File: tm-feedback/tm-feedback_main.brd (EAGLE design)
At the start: 60.1 x 40.3 mm, 45 parts

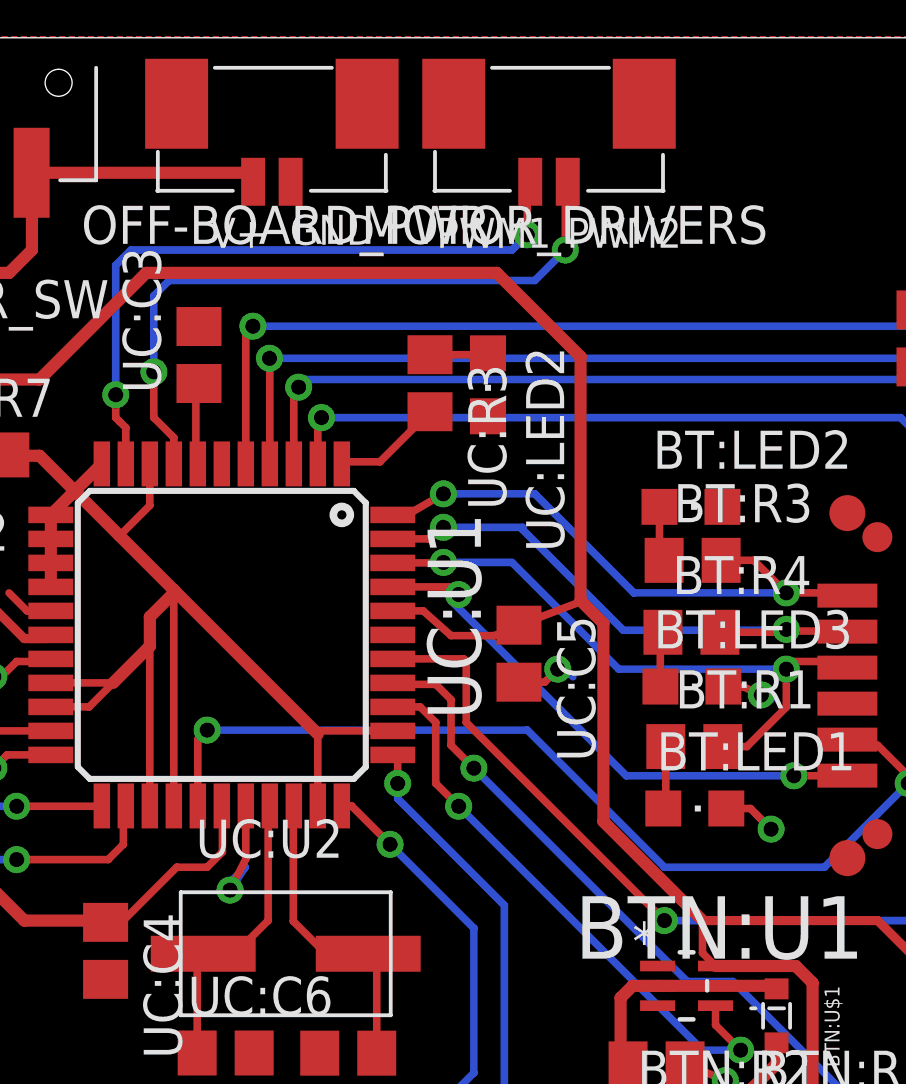
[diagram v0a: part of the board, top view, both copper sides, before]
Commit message: Fix ground vias
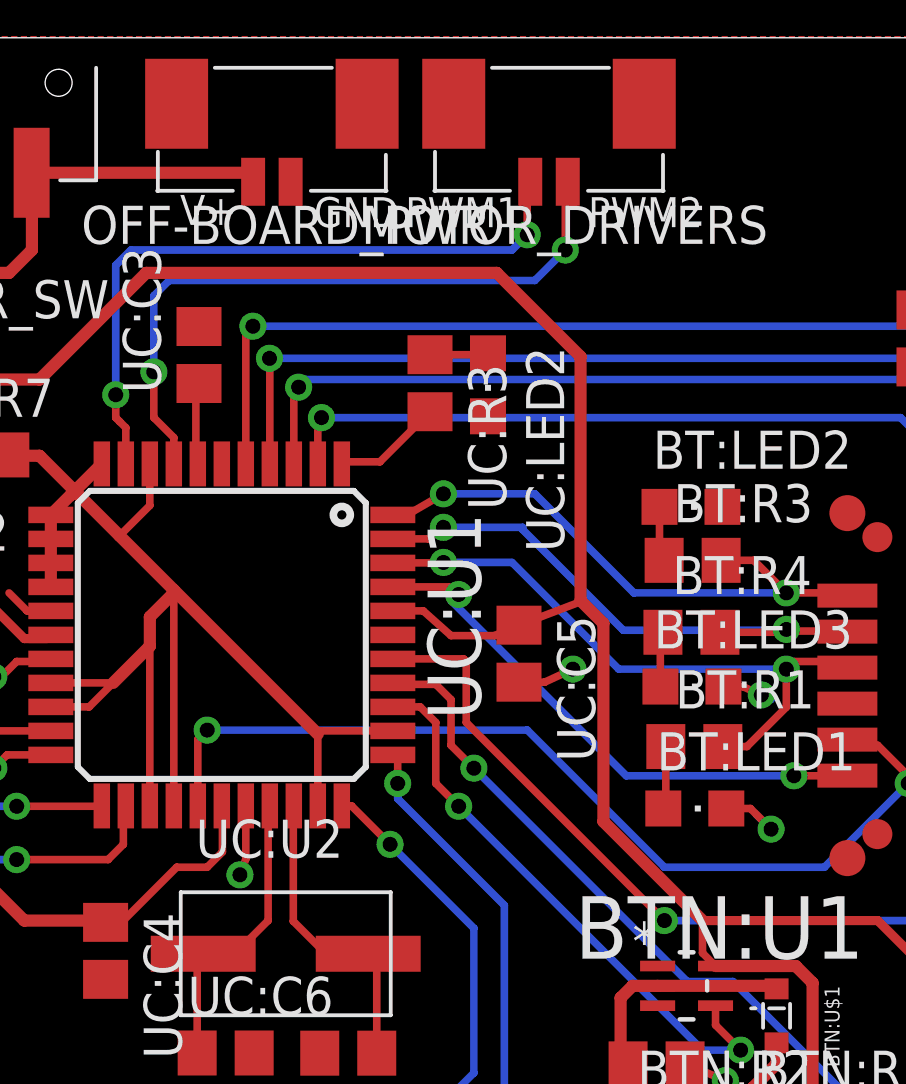
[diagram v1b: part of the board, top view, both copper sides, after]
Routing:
- net GND: track 21.6 -> 19.2 mm
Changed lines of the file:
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@@
 <setting verticaltext="up"/>
 </settings>
-<grid distance="10" unitdist="mil" unit="mil" style="lines" multiple="10" display="yes" altdistance="0.01" altunitdist="mm" altunit="mm"/>
+<grid distance="1" unitdist="mil" unit="mil" style="lines" multiple="10" display="yes" altdistance="0.01" altunitdist="mm" altunit="mm"/>
 <layers>
 <layer number="1" name="Top" color="4" fill="1" visible="yes" active="yes"/>
@@
 <wire x1="60.122" y1="40.348" x2="0" y2="40.348" width="0" layer="20"/>
 <wire x1="0" y1="40.348" x2="0" y2="0" width="0" layer="20"/>
-<text x="24.24" y="33.348" size="1" layer="21" font="vector" ratio="20">V+</text>
-<text x="26.886" y="33.448" size="1" layer="21" font="vector" ratio="20">GND</text>
-<text x="31.778" y="33.348" size="1" layer="21" font="vector" ratio="20">PWM1</text>
-<text x="36.124" y="33.348" size="1" layer="21" font="vector" ratio="20">PWM2</text>
+<text x="23.224" y="34.11" size="1" layer="21" font="vector" ratio="20">V+</text>
+<text x="27.686" y="34.036" size="1" layer="21" font="vector" ratio="20">GND</text>
+<text x="30.734" y="34.036" size="1" layer="21" font="vector" ratio="20">PWM1</text>
+<text x="36.83" y="34.036" size="1" layer="21" font="vector" ratio="20">PWM2</text>
 <text x="5.554" y="34.65" size="1" layer="21" font="vector" ratio="20">+</text>
 <text x="5.5" y="31.192" size="1" layer="21" font="vector" ratio="20">-</text>
@@
 </polygon>
 <wire x1="25.418" y1="14.744" x2="25.418" y2="12.972" width="0.254" layer="1"/>
-<wire x1="25.418" y1="12.972" x2="24.892" y2="11.938" width="0.254" layer="1"/>
-<via x="24.892" y="11.938" extent="1-16" drill="0.5"/>
-<wire x1="24.892" y1="11.938" x2="25.4" y2="12.7" width="0.254" layer="16"/>
-<wire x1="25.4" y1="12.7" x2="24.892" y2="12.192" width="0.254" layer="16"/>
+<wire x1="25.418" y1="12.972" x2="25.2222" y2="12.446" width="0.254" layer="1"/>
+<via x="25.2222" y="12.446" extent="1-16" drill="0.5"/>
 <wire x1="15.652" y1="26.444" x2="15.652" y2="26.32" width="0.254" layer="1"/>
 <wire x1="15.652" y1="26.32" x2="14.478" y2="25.146" width="0.254" layer="1"/>
@@
 <wire x1="41.402" y1="5.588" x2="41.656" y2="5.334" width="0.254" layer="16"/>
 <wire x1="34.524" y1="18.868" x2="35.378" y2="18.868" width="0.254" layer="1"/>
-<wire x1="35.378" y1="18.868" x2="35.814" y2="19.304" width="0.254" layer="1"/>
-<via x="35.814" y="19.304" extent="1-16" drill="0.5"/>
-<wire x1="35.814" y1="19.304" x2="36.068" y2="19.304" width="0.254" layer="16"/>
-<wire x1="36.068" y1="19.304" x2="36.322" y2="19.05" width="0.254" layer="16"/>
+<wire x1="35.378" y1="18.868" x2="36.322" y2="19.304" width="0.254" layer="1"/>
+<via x="36.322" y="19.304" extent="1-16" drill="0.5"/>
 <wire x1="41.434" y1="14.658" x2="42.238" y2="14.658" width="0.254" layer="1"/>
 <wire x1="42.238" y1="14.658" x2="42.926" y2="13.97" width="0.254" layer="1"/>

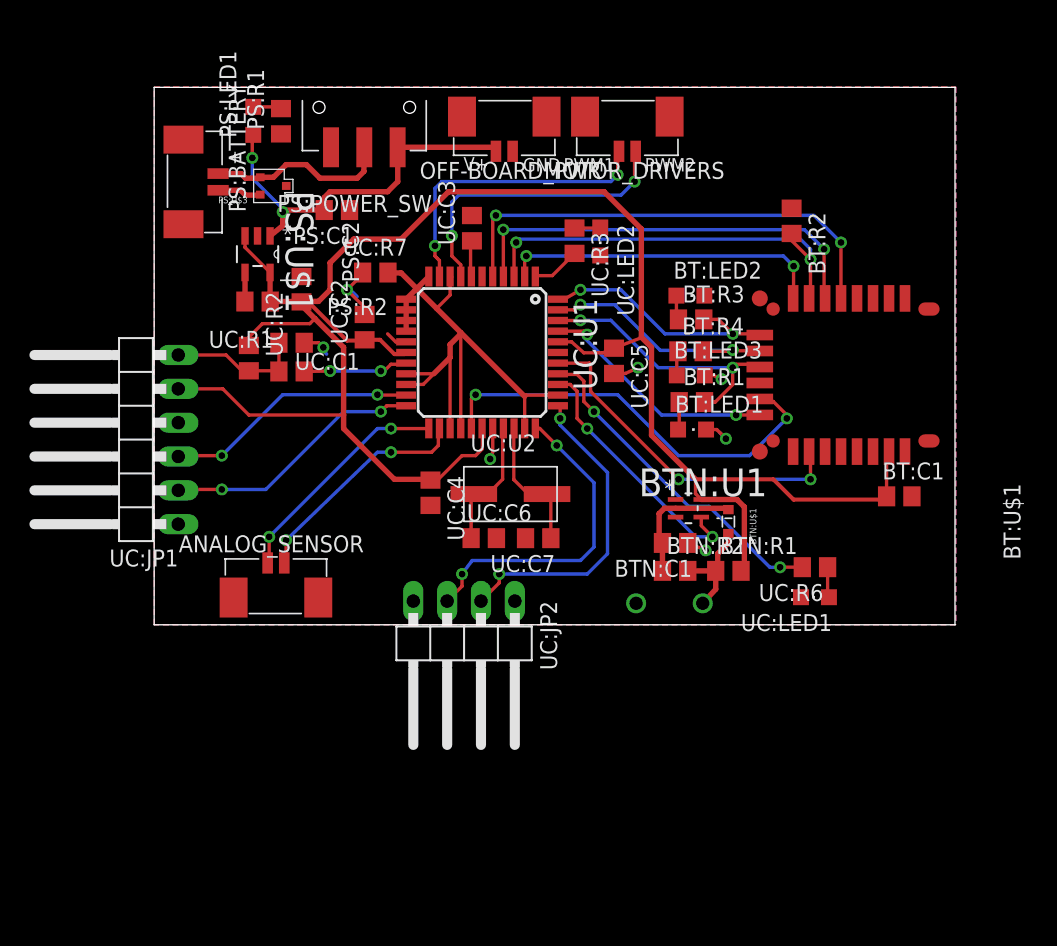
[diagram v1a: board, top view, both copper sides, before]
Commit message: Fix more ground vias
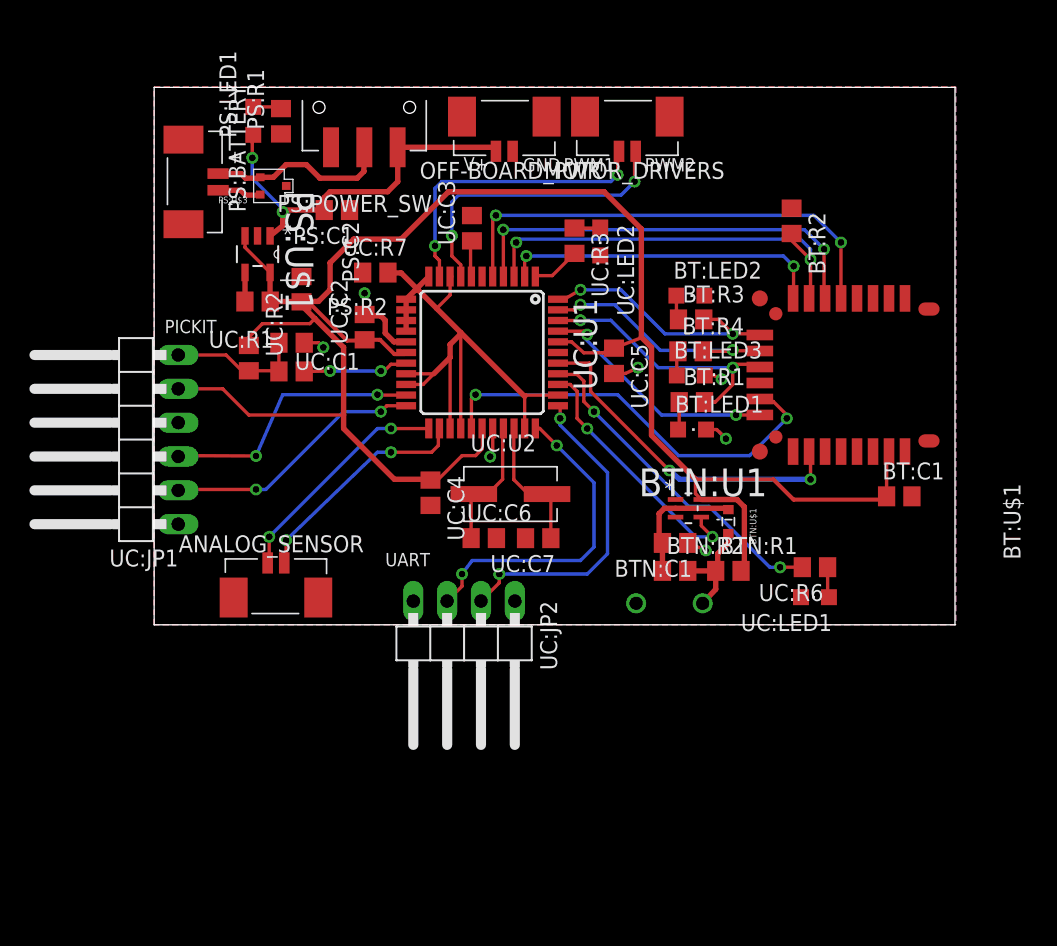
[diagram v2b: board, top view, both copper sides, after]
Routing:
- net GND: track 19.2 -> 16.8 mm
- net UC:PGD: track 19.0 -> 20.2 mm
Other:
- board text added: "PICKIT"
- board text added: "UART"
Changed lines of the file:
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@@
 <layer number="20" name="Dimension" color="15" fill="1" visible="yes" active="yes"/>
 <layer number="21" name="tPlace" color="7" fill="1" visible="yes" active="yes"/>
-<layer number="22" name="bPlace" color="7" fill="1" visible="yes" active="yes"/>
+<layer number="22" name="bPlace" color="7" fill="1" visible="no" active="yes"/>
 <layer number="23" name="tOrigins" color="15" fill="1" visible="no" active="yes"/>
 <layer number="24" name="bOrigins" color="15" fill="1" visible="no" active="yes"/>
@@
 <layer number="27" name="tValues" color="7" fill="1" visible="no" active="yes"/>
 <layer number="28" name="bValues" color="7" fill="1" visible="no" active="yes"/>
-<layer number="29" name="tStop" color="7" fill="3" visible="no" active="yes"/>
+<layer number="29" name="tStop" color="7" fill="3" visible="yes" active="yes"/>
 <layer number="30" name="bStop" color="7" fill="6" visible="no" active="yes"/>
 <layer number="31" name="tCream" color="7" fill="4" visible="no" active="yes"/>
@@
 <layer number="38" name="bTest" color="7" fill="1" visible="no" active="yes"/>
 <layer number="39" name="tKeepout" color="4" fill="11" visible="yes" active="yes"/>
-<layer number="40" name="bKeepout" color="1" fill="11" visible="yes" active="yes"/>
+<layer number="40" name="bKeepout" color="1" fill="11" visible="no" active="yes"/>
 <layer number="41" name="tRestrict" color="4" fill="10" visible="yes" active="yes"/>
-<layer number="42" name="bRestrict" color="1" fill="10" visible="yes" active="yes"/>
-<layer number="43" name="vRestrict" color="2" fill="10" visible="yes" active="yes"/>
-<layer number="44" name="Drills" color="7" fill="1" visible="yes" active="yes"/>
-<layer number="45" name="Holes" color="7" fill="1" visible="yes" active="yes"/>
-<layer number="46" name="Milling" color="3" fill="1" visible="yes" active="yes"/>
+<layer number="42" name="bRestrict" color="1" fill="10" visible="no" active="yes"/>
+<layer number="43" name="vRestrict" color="2" fill="10" visible="no" active="yes"/>
+<layer number="44" name="Drills" color="7" fill="1" visible="no" active="yes"/>
+<layer number="45" name="Holes" color="7" fill="1" visible="no" active="yes"/>
+<layer number="46" name="Milling" color="3" fill="1" visible="no" active="yes"/>
 <layer number="47" name="Measures" color="7" fill="1" visible="no" active="yes"/>
 <layer number="48" name="Document" color="7" fill="1" visible="no" active="yes"/>
 <layer number="49" name="Reference" color="7" fill="1" visible="no" active="yes"/>
 <layer number="50" name="dxf" color="7" fill="1" visible="no" active="no"/>
-<layer number="51" name="tDocu" color="7" fill="1" visible="yes" active="yes"/>
-<layer number="52" name="bDocu" color="7" fill="1" visible="yes" active="yes"/>
+<layer number="51" name="tDocu" color="7" fill="1" visible="no" active="yes"/>
+<layer number="52" name="bDocu" color="7" fill="1" visible="no" active="yes"/>
 <layer number="90" name="Modules" color="5" fill="1" visible="no" active="no"/>
 <layer number="91" name="Nets" color="2" fill="1" visible="no" active="no"/>
@@
 <layer number="98" name="Guide" color="6" fill="1" visible="no" active="no"/>
 <layer number="99" name="SpiceOrder" color="5" fill="1" visible="no" active="no"/>
+<layer number="200" name="200bmp" color="1" fill="10" visible="yes" active="yes"/>
+<layer number="201" name="201bmp" color="2" fill="10" visible="yes" active="yes"/>
 </layers>
 <board>
@@
 <text x="5.554" y="34.65" size="1" layer="21" font="vector" ratio="20">+</text>
 <text x="5.5" y="31.192" size="1" layer="21" font="vector" ratio="20">-</text>
+<text x="0.7874" y="21.8948" size="1" layer="21" ratio="20">PICKIT</text>
+<text x="17.3482" y="4.3942" size="1" layer="21" ratio="20">UART</text>
 </plain>
 <attributes>
@@
 <vertex x="0" y="0"/>
 </polygon>
-<wire x1="25.418" y1="14.744" x2="25.418" y2="12.972" width="0.254" layer="1"/>
-<wire x1="25.418" y1="12.972" x2="25.2222" y2="12.446" width="0.254" layer="1"/>
-<via x="25.2222" y="12.446" extent="1-16" drill="0.5"/>
+<wire x1="25.418" y1="14.744" x2="25.418" y2="13.1498" width="0.254" layer="1"/>
+<wire x1="25.418" y1="13.1498" x2="25.2222" y2="12.6238" width="0.254" layer="1"/>
+<via x="25.2222" y="12.6238" extent="1-16" drill="0.5"/>
 <wire x1="15.652" y1="26.444" x2="15.652" y2="26.32" width="0.254" layer="1"/>
-<wire x1="15.652" y1="26.32" x2="14.478" y2="25.146" width="0.254" layer="1"/>
-<via x="14.478" y="25.146" extent="1-16" drill="0.5"/>
-<wire x1="14.478" y1="25.146" x2="14.732" y2="25.146" width="0.254" layer="16"/>
-<wire x1="14.732" y1="25.146" x2="15.24" y2="24.638" width="0.254" layer="16"/>
+<via x="15.7988" y="24.892" extent="1-16" drill="0.5"/>
 <wire x1="15.8" y1="23.296" x2="15.8" y2="23.824" width="0.254" layer="1"/>
-<wire x1="15.8" y1="23.824" x2="14.478" y2="25.146" width="0.254" layer="1"/>
-<wire x1="18.918" y1="21.244" x2="18.126" y2="21.244" width="0.254" layer="1"/>
-<wire x1="18.126" y1="21.244" x2="17.526" y2="21.844" width="0.254" layer="1"/>
 <wire x1="11.266" y1="21.174" x2="12.354" y2="21.174" width="0.254" layer="1"/>
 <wire x1="12.354" y1="21.174" x2="12.7" y2="20.828" width="0.254" layer="1"/>
 <via x="12.7" y="20.828" extent="1-16" drill="0.5"/>
-<wire x1="12.7" y1="20.828" x2="12.7" y2="20.574" width="0.254" layer="16"/>
-<wire x1="12.7" y1="20.574" x2="12.954" y2="20.32" width="0.254" layer="16"/>
 <wire x1="40.06" y1="6.146" x2="40.082" y2="6.146" width="0.254" layer="1"/>
 <wire x1="40.082" y1="6.146" x2="41.402" y2="5.588" width="0.254" layer="1"/>
@@
 <via x="42.602" y="18.442" extent="1-16" drill="0.5"/>
 <wire x1="42.602" y1="18.442" x2="42.926" y2="18.288" width="0.254" layer="16"/>
+<wire x1="18.918" y1="21.244" x2="17.999" y2="21.244" width="0.4064" layer="1"/>
+<wire x1="17.999" y1="21.244" x2="17.3482" y2="21.8948" width="0.4064" layer="1"/>
+<wire x1="17.3482" y1="21.8948" x2="17.3482" y2="22.86" width="0.4064" layer="1"/>
+<wire x1="17.3482" y1="22.86" x2="17.018" y2="23.1902" width="0.4064" layer="1"/>
+<wire x1="17.018" y1="23.1902" x2="15.9058" y2="23.1902" width="0.4064" layer="1"/>
+<wire x1="15.9058" y1="23.1902" x2="15.8" y2="23.296" width="0.4064" layer="1"/>
 </signal>
 <signal name="BT:N$6">
@@
 <via x="16.764" y="17.272" extent="1-16" drill="0.5"/>
 <wire x1="16.764" y1="17.272" x2="9.652" y2="17.272" width="0.254" layer="16"/>
-<wire x1="9.652" y1="17.272" x2="5.08" y2="12.7" width="0.254" layer="16"/>
-<via x="5.08" y="12.7" extent="1-16" drill="0.5"/>
-<wire x1="5.08" y1="12.7" x2="1.876" y2="12.7" width="0.254" layer="1"/>
+<wire x1="9.652" y1="17.272" x2="7.6454" y2="12.6746" width="0.254" layer="16"/>
+<via x="7.6454" y="12.6746" extent="1-16" drill="0.5"/>
+<wire x1="7.6454" y1="12.6746" x2="1.876" y2="12.7" width="0.254" layer="1"/>
 <wire x1="1.876" y1="12.7" x2="1.81" y2="12.634" width="0.254" layer="1"/>
 </signal>
@@
 <wire x1="17.46" y1="16.444" x2="17.018" y2="16.002" width="0.254" layer="1"/>
 <via x="17.018" y="16.002" extent="1-16" drill="0.5"/>
-<via x="5.08" y="10.16" extent="1-16" drill="0.5"/>
-<wire x1="5.08" y1="10.16" x2="1.876" y2="10.16" width="0.254" layer="1"/>
+<via x="7.6454" y="10.16" extent="1-16" drill="0.5"/>
+<wire x1="7.6454" y1="10.16" x2="1.876" y2="10.16" width="0.254" layer="1"/>
 <wire x1="1.876" y1="10.16" x2="1.81" y2="10.094" width="0.254" layer="1"/>
-<wire x1="5.08" y1="10.16" x2="8.382" y2="10.16" width="0.254" layer="16"/>
+<wire x1="7.6454" y1="10.16" x2="8.382" y2="10.16" width="0.254" layer="16"/>
 <wire x1="8.382" y1="10.16" x2="14.224" y2="16.002" width="0.254" layer="16"/>
 <wire x1="14.224" y1="16.002" x2="17.018" y2="16.002" width="0.254" layer="16"/>
@@
 <wire x1="32.68" y1="19.644" x2="32.766" y2="19.558" width="0.254" layer="1"/>
 <wire x1="32.766" y1="19.558" x2="32.766" y2="17.526" width="0.254" layer="1"/>
-<wire x1="32.766" y1="17.526" x2="39.37" y2="10.922" width="0.254" layer="1"/>
-<via x="39.37" y="10.922" extent="1-16" drill="0.5"/>
-<wire x1="39.37" y1="10.922" x2="49.276" y2="10.922" width="0.254" layer="16"/>
+<wire x1="32.766" y1="17.526" x2="38.6842" y2="11.5824" width="0.254" layer="1"/>
+<via x="38.6842" y="11.5824" extent="1-16" drill="0.5"/>
+<wire x1="38.6842" y1="11.5824" x2="39.4462" y2="10.922" width="0.4064" layer="16"/>
+<wire x1="39.4462" y1="10.922" x2="49.276" y2="10.922" width="0.4064" layer="16"/>
 </signal>
 <signal name="N$7">
